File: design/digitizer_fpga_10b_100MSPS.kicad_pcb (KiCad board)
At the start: 4 copper layers, 125 x 60 mm, 284 parts, among them J1 POWER, J2 SWD_01X04, J3 DEBUG_SPI, J4 USB_B_Mini, J5 SMA, J6 JUMPER_DFS/GAIN, J7 DEBUG_FPGA_GPIO, J8 DIGILENT_JTAG_HS2_01X06, SW1 RST, SW2 PROG, U1 LM3880MF-1AA, U10 IS61WV12816EDBLL-10TLI, U11 TLV431ACDBZR, U12 AD9214, U13 XC7S15-FTGB196, U14 IS25LP064A-JKx, U2 NCP59744MN1, U3 NCP59744MN1, U4 NCP59744MN1, U5 NCP59744MN1, U6 STM32H750VBTx, U7 USBLC6-2SC6, U8 FT231XS, U9 ADA4930-1, X1 ASTX-H11-25.000MHZ-T

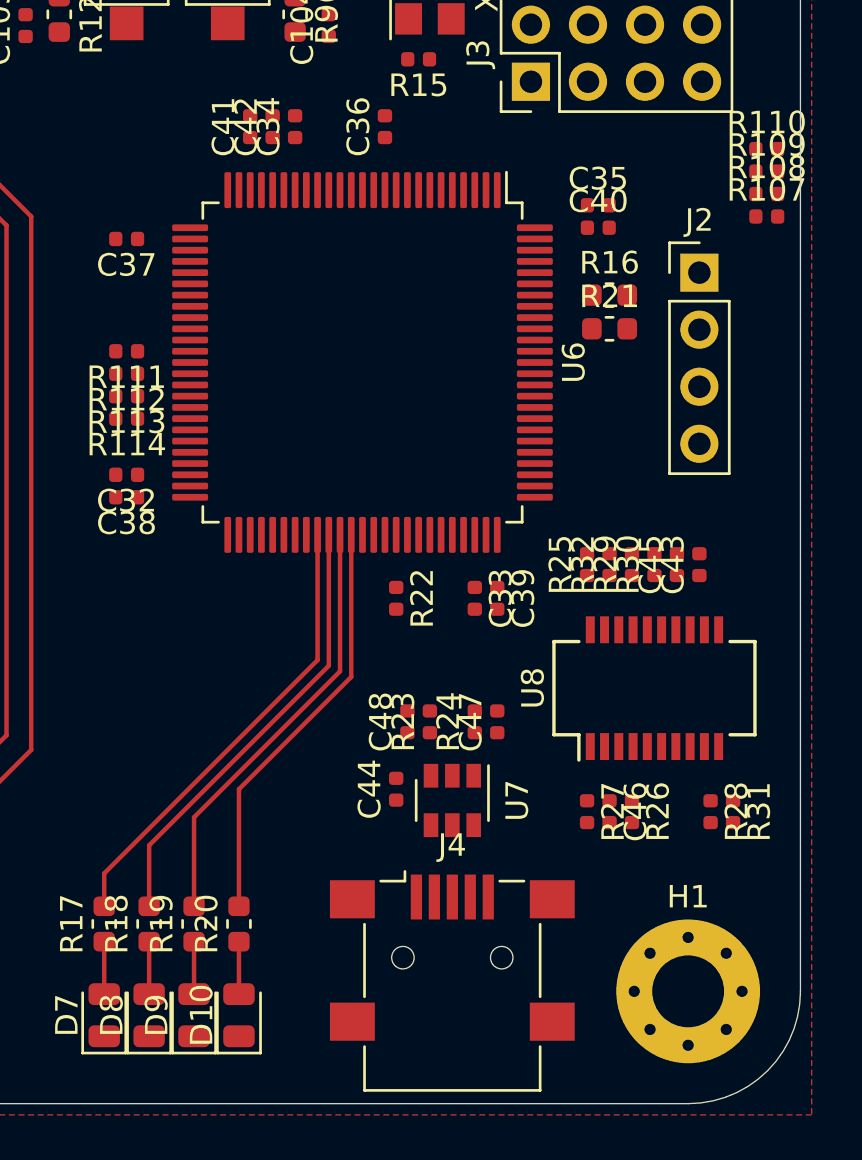
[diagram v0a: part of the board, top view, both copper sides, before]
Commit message: Added FTDI layout
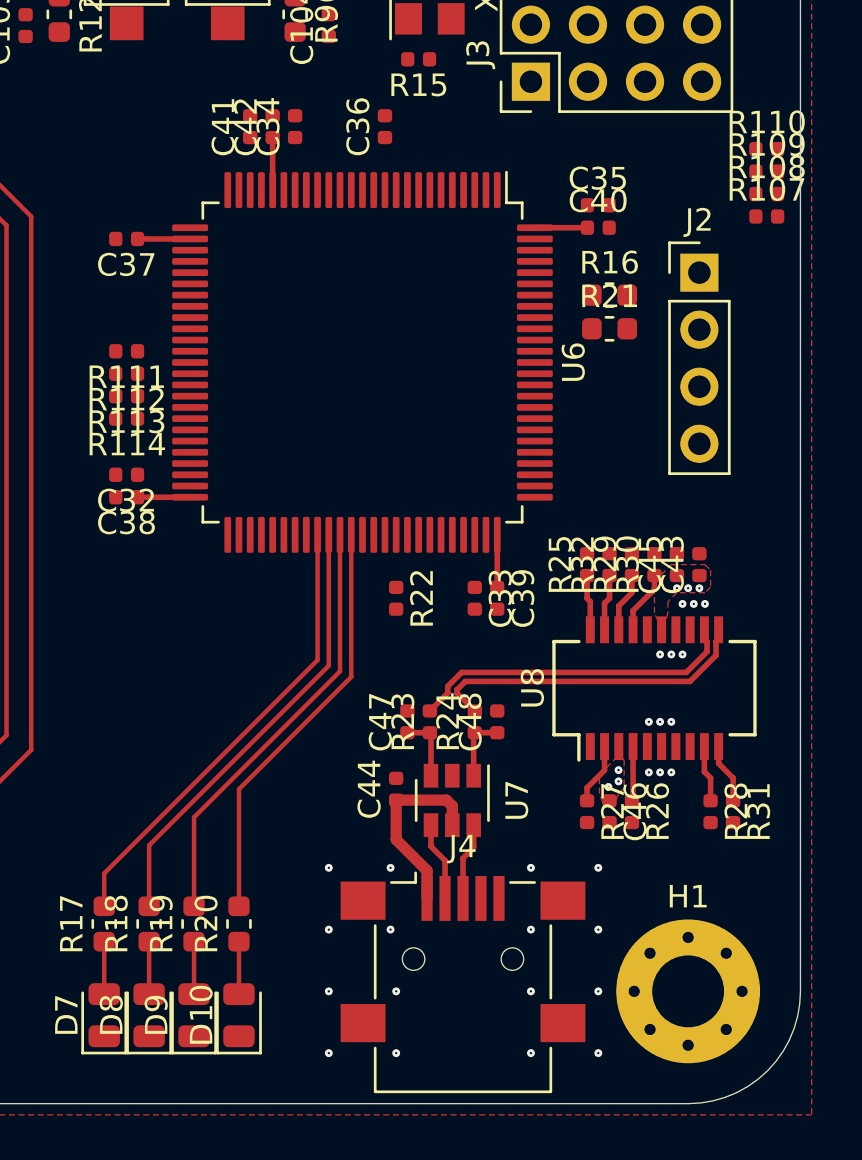
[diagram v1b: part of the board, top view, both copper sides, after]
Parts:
- moved C47 4.00 mm to (177.5, 133.0)
- moved C48 4.00 mm to (181.5, 133.0)
- moved J4 0.48 mm to (180.0, 143.6)
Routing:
- net /USB/D-: track 0.00 -> 14.6 mm
- net /USB/D+: track 0.00 -> 14.6 mm
- net +3V3D: track 25.4 -> 37.1 mm, vias 19 -> 25
- net /USB/VBUS: track 0.00 -> 8.41 mm
- net /USB/USB-: track 0.00 -> 3.73 mm
- net /USB/USB+: track 0.00 -> 3.46 mm
- net /USB/DATA-: track 0.00 -> 2.94 mm
- net /USB/DATA+: track 0.00 -> 2.94 mm
- net Net-(R30-Pad1): track 0.00 -> 2.81 mm
- net Net-(R27-Pad1): track 0.00 -> 2.74 mm
- net Net-(R31-Pad1): track 0.00 -> 2.68 mm
- net Net-(R29-Pad1): track 0.00 -> 2.66 mm
- net Net-(R28-Pad1): track 0.00 -> 2.53 mm
- net Net-(R32-Pad1): track 0.00 -> 2.51 mm
- net Net-(R25-Pad1): track 0.00 -> 2.47 mm
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
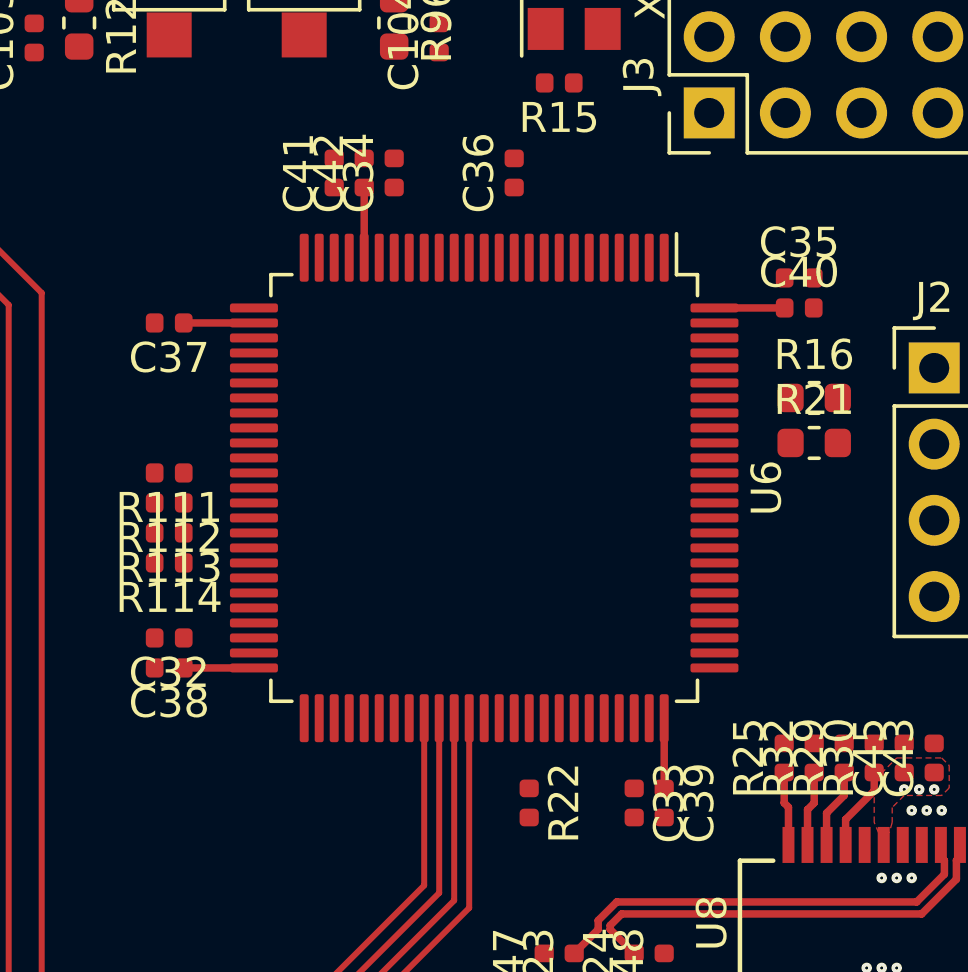
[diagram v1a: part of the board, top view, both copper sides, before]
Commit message: Added MCU power layout
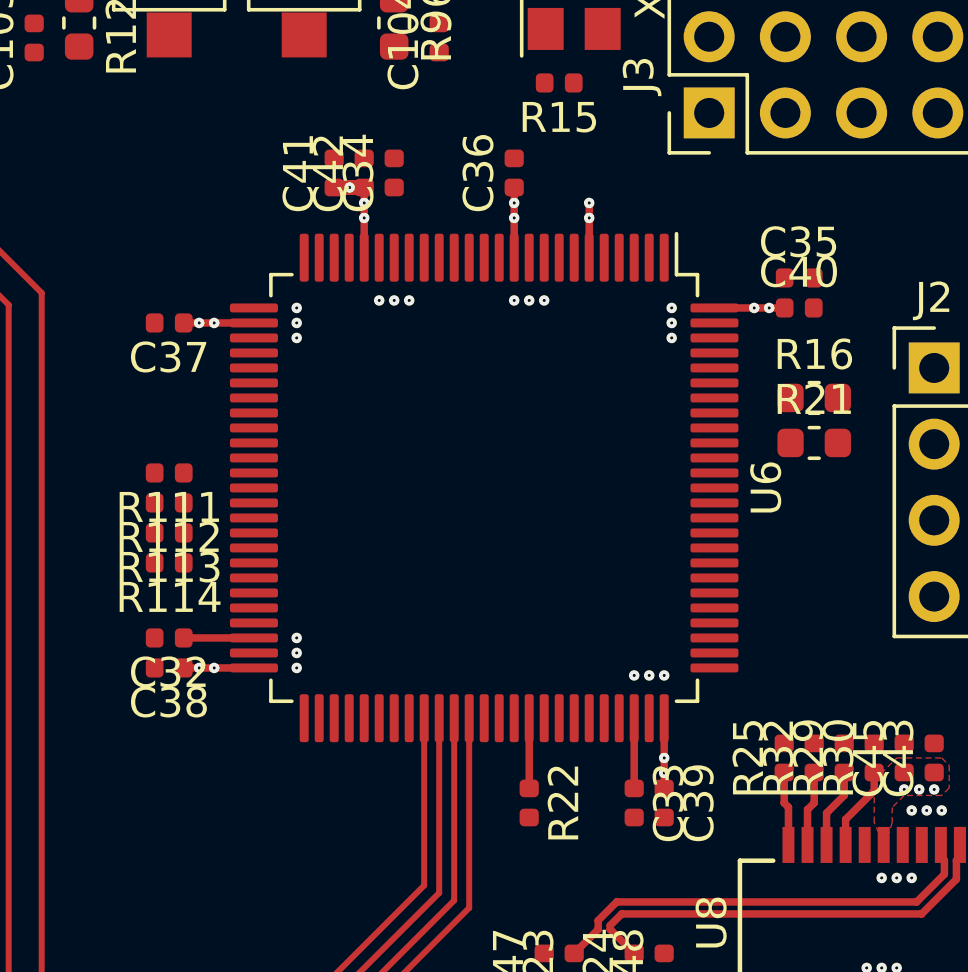
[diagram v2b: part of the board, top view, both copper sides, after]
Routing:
- net +3V3D: track 37.1 -> 42.2 mm, vias 25 -> 40
- net Net-(R22-Pad1): track 0.00 -> 2.34 mm
- net Net-(C33-Pad1): track 0.00 -> 2.34 mm
- net Net-(C32-Pad1): track 0.00 -> 2.34 mm
- net GND: vias 157 -> 175
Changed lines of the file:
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@@
     (thickness 1.628)
     (drawings 36)
-    (tracks 1101)
+    (tracks 1154)
     (modules 284)
     (nets 354)
@@
   (gr_line (start 75 90) (end 190 90) (layer "Edge.Cuts") (width 0.05))
   (gr_line (start 70 145) (end 70 95) (layer "Edge.Cuts") (width 0.05))
-  (segment (start 171.5 109.325) (end 171.5 106.985) (width 0.25) (layer "TOP") (net 2))
-  (segment (start 167.825 111.5) (end 165.485 111.5) (width 0.25) (layer "TOP") (net 2))
-  (segment (start 167.825 123) (end 165.485 123) (width 0.25) (layer "TOP") (net 2))
-  (segment (start 181.5 124.675) (end 181.5 127.015) (width 0.25) (layer "TOP") (net 2))
-  (segment (start 183.175 111) (end 185.515 111) (width 0.25) (layer "TOP") (net 2))
+  (via (at 169.25 112) (size 0.35) (drill 0.1) (layers "TOP" "BOT") (net 1))
+  (via (at 173 110.75) (size 0.35) (drill 0.1) (layers "TOP" "BOT") (net 1))
+  (via (at 169.25 111.5) (size 0.35) (drill 0.1) (layers "TOP" "BOT") (net 1))
+  (via (at 169.25 111) (size 0.35) (drill 0.1) (layers "TOP" "BOT") (net 1))
+  (via (at 169.25 122) (size 0.35) (drill 0.1) (layers "TOP" "BOT") (net 1))
+  (via (at 169.25 123) (size 0.35) (drill 0.1) (layers "TOP" "BOT") (net 1))
+  (via (at 169.25 122.5) (size 0.35) (drill 0.1) (layers "TOP" "BOT") (net 1))
+  (via (at 180.5 123.25) (size 0.35) (drill 0.1) (layers "TOP" "BOT") (net 1))
+  (via (at 181.5 123.25) (size 0.35) (drill 0.1) (layers "TOP" "BOT") (net 1))
+  (via (at 181 123.25) (size 0.35) (drill 0.1) (layers "TOP" "BOT") (net 1))
+  (via (at 181.75 112) (size 0.35) (drill 0.1) (layers "TOP" "BOT") (net 1))
+  (via (at 181.75 111) (size 0.35) (drill 0.1) (layers "TOP" "BOT") (net 1))
+  (via (at 181.75 111.5) (size 0.35) (drill 0.1) (layers "TOP" "BOT") (net 1))
+  (via (at 172 110.75) (size 0.35) (drill 0.1) (layers "TOP" "BOT") (net 1))
+  (via (at 172.5 110.75) (size 0.35) (drill 0.1) (layers "TOP" "BOT") (net 1))
+  (via (at 176.5 110.75) (size 0.35) (drill 0.1) (layers "TOP" "BOT") (net 1))
+  (via (at 177.5 110.75) (size 0.35) (drill 0.1) (layers "TOP" "BOT") (net 1))
+  (via (at 177 110.75) (size 0.35) (drill 0.1) (layers "TOP" "BOT") (net 1))
+  (via (at 171.5 108) (size 0.35) (drill 0.1) (layers "TOP" "BOT") (net 2))
+  (segment (start 171.5 108) (end 171.5 107.5) (width 0.25) (layer "TOP") (net 2))
+  (segment (start 171.5 109.325) (end 171.5 108) (width 0.25) (layer "TOP") (net 2))
+  (segment (start 171.5 107.5) (end 171.5 106.985) (width 0.25) (layer "TOP") (net 2))
+  (via (at 171.5 107.5) (size 0.35) (drill 0.1) (layers "TOP" "BOT") (net 2))
+  (via (at 176.5 108) (size 0.35) (drill 0.1) (layers "TOP" "BOT") (net 2))
+  (segment (start 176.5 107.5) (end 176.5 108) (width 0.25) (layer "TOP") (net 2))
+  (segment (start 176.5 108) (end 176.5 109.325) (width 0.25) (layer "TOP") (net 2))
+  (via (at 176.5 107.5) (size 0.35) (drill 0.1) (layers "TOP" "BOT") (net 2))
+  (segment (start 176.5 106.985) (end 176.5 107.5) (width 0.25) (layer "TOP") (net 2))
+  (via (at 179 108) (size 0.35) (drill 0.1) (layers "TOP" "BOT") (net 2))
+  (segment (start 179 108) (end 179 107.5) (width 0.25) (layer "TOP") (net 2))
+  (segment (start 179 109.325) (end 179 108) (width 0.25) (layer "TOP") (net 2))
+  (via (at 179 107.5) (size 0.35) (drill 0.1) (layers "TOP" "BOT") (net 2))
+  (via (at 184.5 111) (size 0.35) (drill 0.1) (layers "TOP" "BOT") (net 2))
+  (segment (start 183.175 111) (end 184.5 111) (width 0.25) (layer "TOP") (net 2))
+  (segment (start 184.5 111) (end 185 111) (width 0.25) (layer "TOP") (net 2))
+  (segment (start 185 111) (end 185.515 111) (width 0.25) (layer "TOP") (net 2))
+  (via (at 185 111) (size 0.35) (drill 0.1) (layers "TOP" "BOT") (net 2))
+  (via (at 166.5 123) (size 0.35) (drill 0.1) (layers "TOP" "BOT") (net 2))
+  (segment (start 166.5 123) (end 166 123) (width 0.25) (layer "TOP") (net 2))
+  (segment (start 167.825 123) (end 166.5 123) (width 0.25) (layer "TOP") (net 2))
+  (segment (start 166 123) (end 165.485 123) (width 0.25) (layer "TOP") (net 2))
+  (via (at 166 123) (size 0.35) (drill 0.1) (layers "TOP" "BOT") (net 2))
+  (via (at 166.5 111.5) (size 0.35) (drill 0.1) (layers "TOP" "BOT") (net 2))
+  (segment (start 166.5 111.5) (end 166 111.5) (width 0.25) (layer "TOP") (net 2))
+  (segment (start 167.825 111.5) (end 166.5 111.5) (width 0.25) (layer "TOP") (net 2))
+  (segment (start 166 111.5) (end 165.485 111.5) (width 0.25) (layer "TOP") (net 2))
+  (via (at 166 111.5) (size 0.35) (drill 0.1) (layers "TOP" "BOT") (net 2))
+  (via (at 171.015 106.985) (size 0.35) (drill 0.1) (layers "TOP" "BOT") (net 2))
+  (segment (start 171.015 106.985) (end 170.5 106.985) (width 0.5) (layer "TOP") (net 2))
+  (segment (start 171.5 106.985) (end 171.015 106.985) (width 0.5) (layer "TOP") (net 2))
+  (segment (start 165.485 122) (end 167.825 122) (width 0.25) (layer "TOP") (net 112))
+  (segment (start 177 124.675) (end 177 127.015) (width 0.25) (layer "TOP") (net 49))
+  (segment (start 180.5 124.675) (end 180.5 127.015) (width 0.25) (layer "TOP") (net 113))
+  (via (at 181.5 126.5) (size 0.35) (drill 0.1) (layers "TOP" "BOT") (net 2))
+  (segment (start 181.5 126.5) (end 181.5 127.015) (width 0.25) (layer "TOP") (net 2))
+  (via (at 181.5 126) (size 0.35) (drill 0.1) (layers "TOP" "BOT") (net 2))
+  (segment (start 181.5 126) (end 181.5 126.5) (width 0.25) (layer "TOP") (net 2))
+  (segment (start 181.5 124.675) (end 181.5 126) (width 0.25) (layer "TOP") (net 2))
   (via (at 174 145) (size 0.35) (drill 0.1) (layers "TOP" "BOT") (net 1))
   (via (at 177 145) (size 0.35) (drill 0.1) (layers "TOP" "BOT") (net 1))

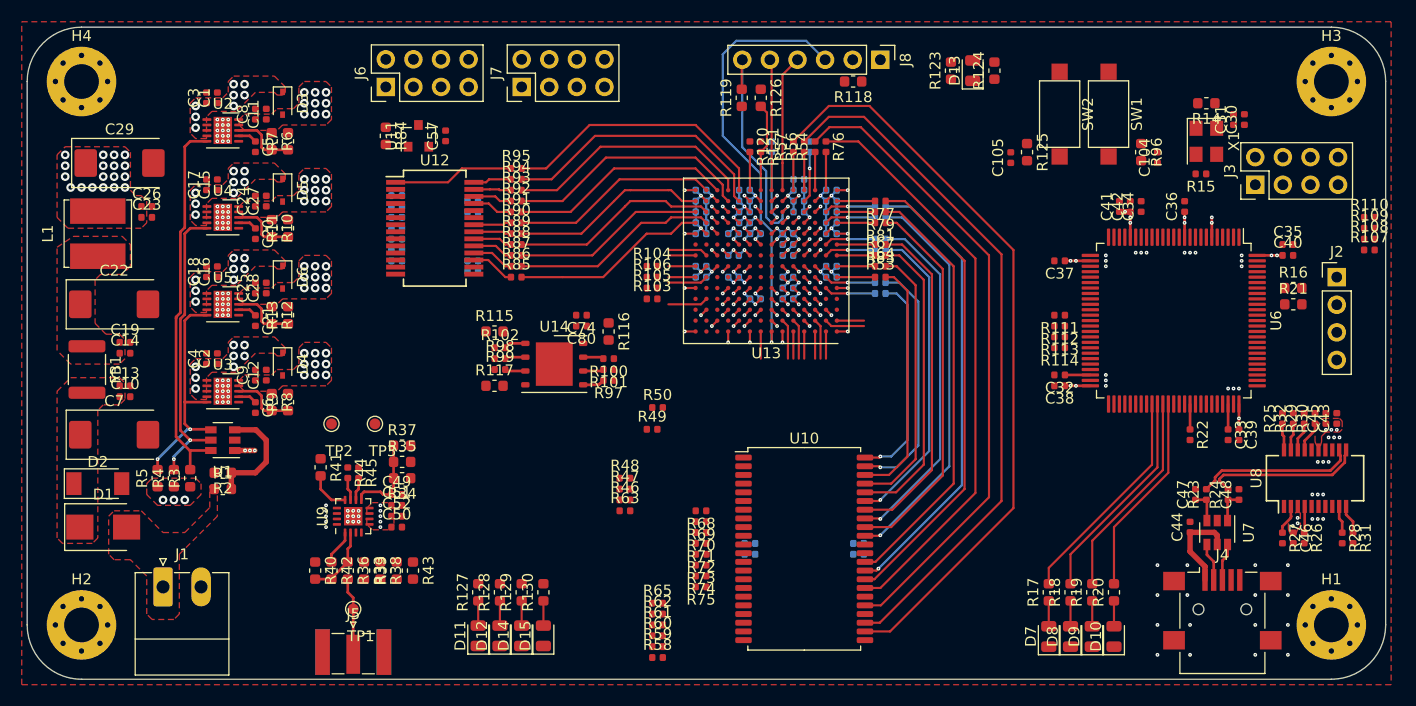
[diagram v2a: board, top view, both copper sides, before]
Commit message: Added LNA layout
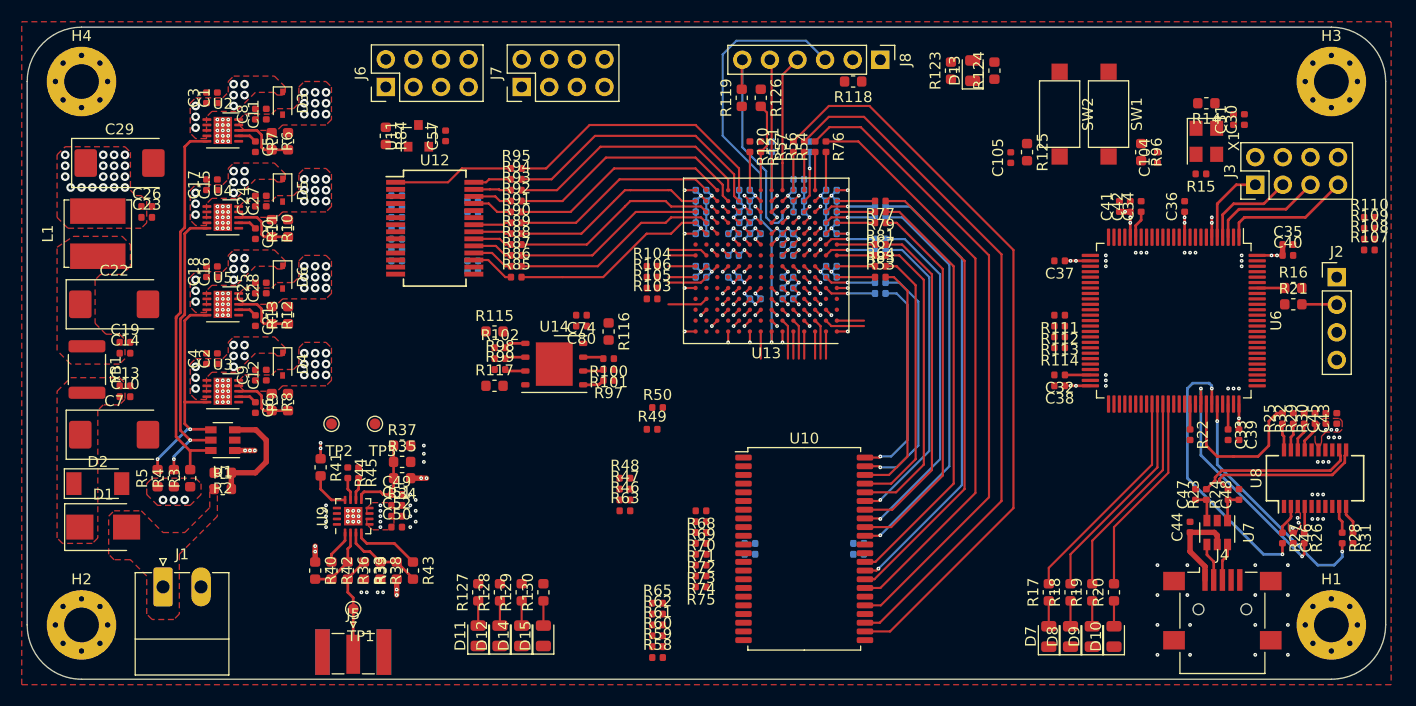
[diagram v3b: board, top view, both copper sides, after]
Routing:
- net /~FTDI_RTS: track 0.00 -> 25.2 mm, vias 0 -> 2
- net /~FTDI_CTS: track 0.00 -> 22.5 mm, vias 0 -> 2
- net /FTDI_RX: track 0.00 -> 22.0 mm, vias 0 -> 2
- net /FTDI_TX: track 0.00 -> 14.2 mm
- net /BRIDGE_SCK: track 0.00 -> 11.9 mm
- net /BRIDGE_NSS: track 0.00 -> 10.5 mm
- net /BRIDGE_MISO: track 0.00 -> 8.75 mm
- net Net-(R38-Pad1): track 0.00 -> 7.66 mm
- net /BRIDGE_MOSI: track 0.00 -> 7.30 mm
- net Net-(R43-Pad1): track 0.00 -> 6.17 mm
- net +3V3A: track 0.00 -> 5.85 mm, vias 14 -> 22
- net /~RST: track 0.71 -> 3.94 mm
- net Net-(C34-Pad1): track 0.00 -> 2.55 mm
- net Net-(R16-Pad1): track 0.00 -> 2.54 mm
- net /LNA/IN: track 7.12 -> 9.32 mm
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- added copper zone on IN3_POWER, net +3V3A

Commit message: Updated some layout
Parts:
- moved D13 62.4 mm to (122.5, 146.0)
- moved R123 62.4 mm to (120.5, 146.0)
- moved R124 62.4 mm to (124.5, 146.0)
- moved C30 0.71 mm to (181.5, 98.0), turned to 0 degrees
- moved C31 0.71 mm to (181.5, 99.0), turned to 0 degrees
- moved R15 0.27 mm to (178.3, 103.5)
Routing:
- net /~RST: track 3.94 -> 35.2 mm, vias 1 -> 2
- net /MCU/SWDIO: track 0.00 -> 13.9 mm, vias 0 -> 1
- net /MCU/SWCLK: track 0.00 -> 9.36 mm
- net /MCU/MCU_OSC_IN: track 0.00 -> 7.73 mm
- net +3V3D: track 43.2 -> 47.7 mm, vias 40 -> 52
- net Net-(R14-Pad2): track 0.00 -> 2.37 mm
- net Net-(R15-Pad1): track 0.00 -> 2.09 mm

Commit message: Updated polygons
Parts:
- moved R84 21.6 mm to (101.0, 121.5), turned to 0 degrees
- moved U11 19.2 mm to (101.0, 118.5), turned to 180 degrees
- moved C57 17.7 mm to (101.0, 116.0), turned to 180 degrees
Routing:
- net /FPGA/FPGA_DQ2: track 0.71 -> 31.4 mm, vias 1 -> 2
- net /FPGA/FPGA_FCS_B: track 0.71 -> 26.8 mm, vias 1 -> 2
- net /FPGA/FPGA_DQ1: track 0.71 -> 26.6 mm, vias 1 -> 2
- net /FPGA/FPGA_DQ0: track 0.00 -> 14.6 mm
- net /FPGA/FPGA_CCLK: track 2.50 -> 16.9 mm, vias 0 -> 2
- net /FPGA/FPGA_DQ3: track 0.71 -> 14.3 mm, vias 1 -> 2
- net /~FTDI_CTS: track 22.5 -> 20.9 mm
- net /~FTDI_RTS: track 25.2 -> 24.0 mm
